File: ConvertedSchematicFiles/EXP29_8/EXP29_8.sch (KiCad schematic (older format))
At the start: 25 parts, among them U1 uA741, U2 uA741

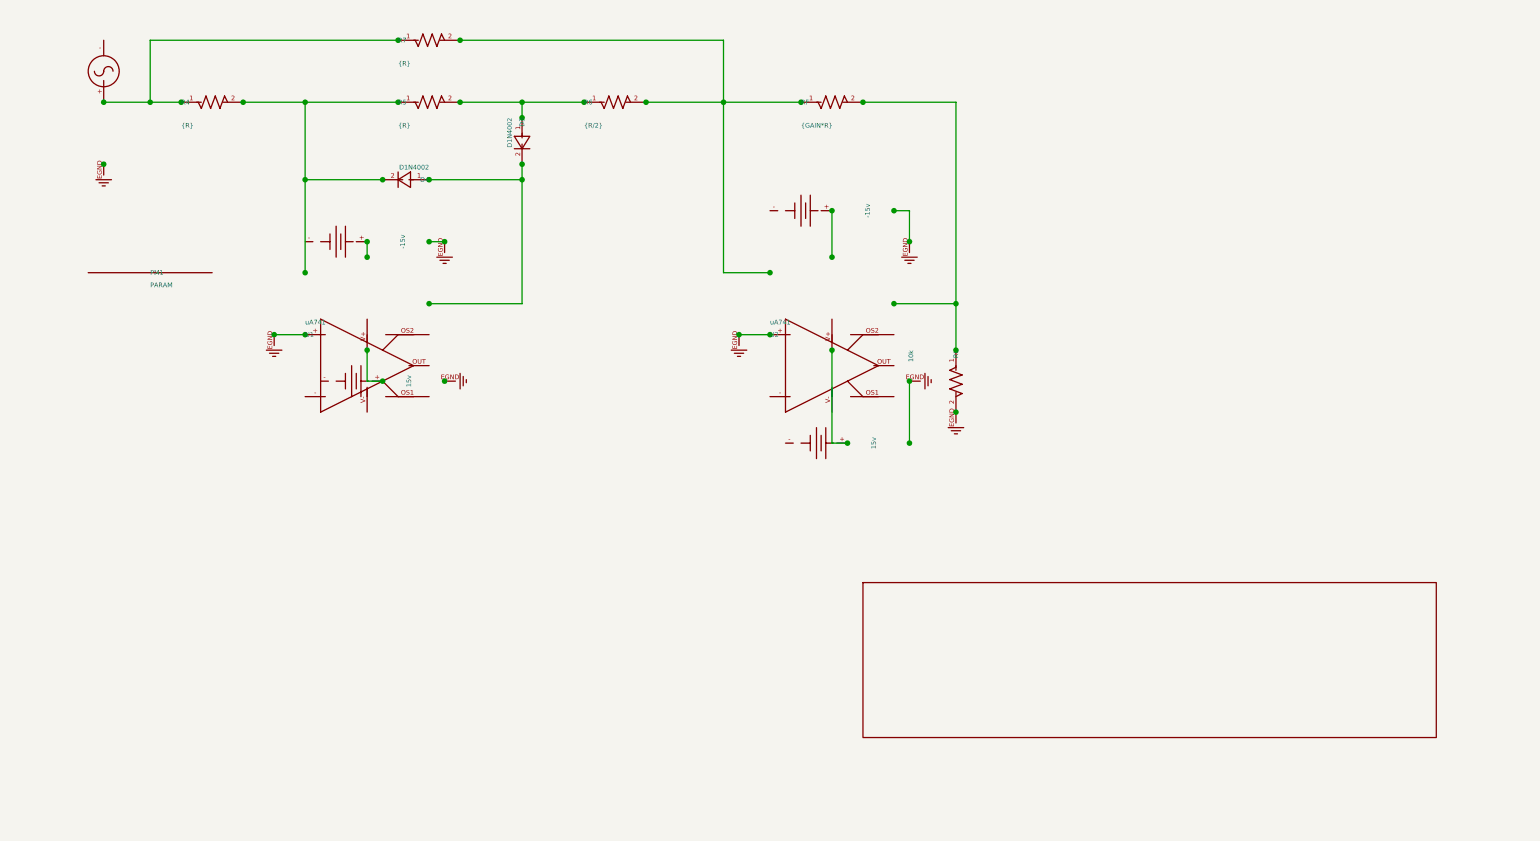
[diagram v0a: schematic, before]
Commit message: Excluded some components. These no longer appear after conversion. When calling shell commands, filenames are in "quotes"
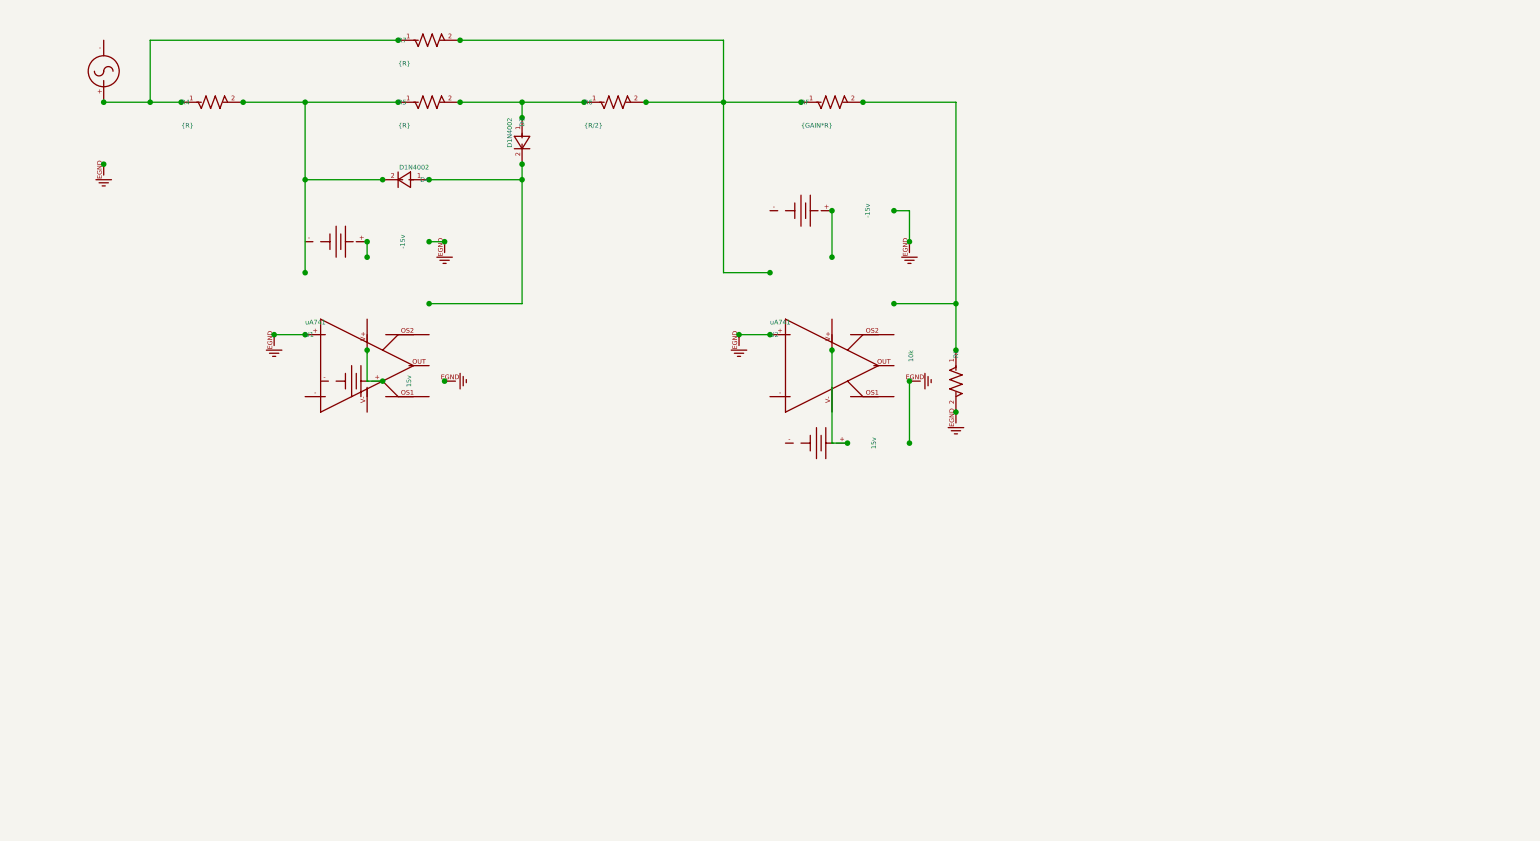
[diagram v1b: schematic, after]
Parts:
- removed PM1: PARAM, symbol PARAM_PSPICE
- removed titleblk: titleblk, symbol TITLEBLK_PSPICE
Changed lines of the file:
@@
 	-1    0    0    -1
-$EndComp
-$Comp
-L PARAM_PSPICE PM1
-U 1 1 26956429
-P 1400 4200
-F 0 "PM1" H 1400 4200 30  0000 L CNN
-F 1 "PARAM" H 1400 4280 30  0000 L CNN
-	1    1400 4200
-	1    0    0    1
-$EndComp
-$Comp
-L TITLEBLK_PSPICE titleblk
-U 1 1 76465782
-P 9700 7200
-F 0 "titleblk" H 19400 14400 30  0001 L CNN
-F 1 "titleblk" H 19400 14480 30  0001 L CNN
-	1    9700 7200
-	1    0    0    1
 $EndComp
 Wire Wire Line

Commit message: Ports issue fixed. Now annotation for ports is #PWR? function added "itos"
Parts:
- removed EGND (x3): EGND, symbol EGND_PSPICE
- removed GND_EARTH (x5): GND_EARTH, symbol GND_EARTH_PSPICE
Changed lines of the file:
@@
 $EndDescr
 $Comp
-L GND_EARTH_PSPICE GND_EARTH
+L GND_EARTH_PSPICE #PWR1
 U 1 1 14289383
 P 3300 4900
-F 0 "GND_EARTH" H 6600 9800 30  0001 L CNN
+F 0 "#PWR1" H 6600 9800 30  0001 L CNN
 F 1 "GND_EARTH" H 6600 9880 30  0001 L CNN
 	1    3300 4900
@@
 $EndComp
 $Comp
-L GND_EARTH_PSPICE GND_EARTH
+L GND_EARTH_PSPICE #PWR2
 U 1 1 46930886
 P 3300 4000
-F 0 "GND_EARTH" H 6600 8000 30  0001 L CNN
+F 0 "#PWR2" H 6600 8000 30  0001 L CNN
 F 1 "GND_EARTH" H 6600 8080 30  0001 L CNN
 	1    3300 4000
@@
 $EndComp
 $Comp
-L GND_EARTH_PSPICE GND_EARTH
+L GND_EARTH_PSPICE #PWR3
 U 1 1 71692777
 P 1100 3500
-F 0 "GND_EARTH" H 2200 7000 30  0001 L CNN
+F 0 "#PWR3" H 2200 7000 30  0001 L CNN
 F 1 "GND_EARTH" H 2200 7080 30  0001 L CNN
 	1    1100 3500
@@
 $EndComp
 $Comp
-L EGND_PSPICE EGND
+L EGND_PSPICE #PWR4
 U 1 1 14636915
 P 6600 5100
-F 0 "EGND" H 13200 10200 30  0001 L CNN
+F 0 "#PWR4" H 13200 10200 30  0001 L CNN
 F 1 "EGND" H 13200 10280 30  0001 L CNN
 	1    6600 5100
@@
 $EndComp
 $Comp
-L EGND_PSPICE EGND
+L EGND_PSPICE #PWR5
 U 1 1 77747793
 P 2200 4600
-F 0 "EGND" H 4400 9200 30  0001 L CNN
+F 0 "#PWR5" H 4400 9200 30  0001 L CNN
 F 1 "EGND" H 4400 9280 30  0001 L CNN
 	1    2200 4600
@@
 $EndComp
 $Comp
-L EGND_PSPICE EGND
+L EGND_PSPICE #PWR6
 U 1 1 74238335
 P 5200 4600
-F 0 "EGND" H 10400 9200 30  0001 L CNN
+F 0 "#PWR6" H 10400 9200 30  0001 L CNN
 F 1 "EGND" H 10400 9280 30  0001 L CNN
 	1    5200 4600
@@
 $EndComp
 $Comp
-L GND_EARTH_PSPICE GND_EARTH
+L GND_EARTH_PSPICE #PWR7
 U 1 1 99885386
 P 6300 4000
-F 0 "GND_EARTH" H 12600 8000 30  0001 L CNN
+F 0 "#PWR7" H 12600 8000 30  0001 L CNN
 F 1 "GND_EARTH" H 12600 8080 30  0001 L CNN
 	1    6300 4000
@@
 $EndComp
 $Comp
-L GND_EARTH_PSPICE GND_EARTH
+L GND_EARTH_PSPICE #PWR8
 U 1 1 39760492
 P 6300 4900
-F 0 "GND_EARTH" H 12600 9800 30  0001 L CNN
+F 0 "#PWR8" H 12600 9800 30  0001 L CNN
 F 1 "GND_EARTH" H 12600 9880 30  0001 L CNN
 	1    6300 4900

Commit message: Added LICENSE.txt
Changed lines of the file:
@@
 $EndDescr
 $Comp
-L GND_EARTH_PSPICE #PWR1
+L GND #PWR1
 U 1 1 14289383
 P 3300 4900
@@
 $EndComp
 $Comp
-L GND_EARTH_PSPICE #PWR2
+L GND #PWR2
 U 1 1 46930886
 P 3300 4000
@@
 $EndComp
 $Comp
-L GND_EARTH_PSPICE #PWR3
+L GND #PWR3
 U 1 1 71692777
 P 1100 3500
@@
 $EndComp
 $Comp
-L EGND_PSPICE #PWR4
+L GND #PWR4
 U 1 1 14636915
 P 6600 5100
@@
 $EndComp
 $Comp
-L EGND_PSPICE #PWR5
+L GND #PWR5
 U 1 1 77747793
 P 2200 4600
@@
 $EndComp
 $Comp
-L EGND_PSPICE #PWR6
+L GND #PWR6
 U 1 1 74238335
 P 5200 4600
@@
 $EndComp
 $Comp
-L GND_EARTH_PSPICE #PWR7
+L GND #PWR7
 U 1 1 99885386
 P 6300 4000
@@
 $EndComp
 $Comp
-L GND_EARTH_PSPICE #PWR8
+L GND #PWR8
 U 1 1 39760492
 P 6300 4900

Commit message: Orientation fix. Library components are now inverted, with +ve y axis going up. In Schematic files, +ve y axis is downwards. This is how the KiCad libraries are. As a result of the above fixed, the converted GND is now oriented correctly.
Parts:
- VIN: value VSIN -> SINE
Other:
- moved on the sheet: U1, U2
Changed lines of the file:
@@
 F 1 "GND_EARTH" H 6600 9880 30  0001 L CNN
 	1    3300 4900
-	0    1    -1    0
+	0    -1    -1    0
 $EndComp
 $Comp
@@
 F 1 "GND_EARTH" H 6600 8080 30  0001 L CNN
 	1    3300 4000
-	1    0    0    1
+	1    0    0    -1
 $EndComp
 $Comp
@@
 F 1 "GND_EARTH" H 2200 7080 30  0001 L CNN
 	1    1100 3500
-	1    0    0    1
+	1    0    0    -1
 $EndComp
 $Comp
@@
 F 1 "EGND" H 13200 10280 30  0001 L CNN
 	1    6600 5100
-	1    0    0    1
+	1    0    0    -1
 $EndComp
 $Comp
@@
 F 1 "EGND" H 4400 9280 30  0001 L CNN
 	1    2200 4600
-	1    0    0    1
+	1    0    0    -1
 $EndComp
 $Comp
@@
 F 1 "EGND" H 10400 9280 30  0001 L CNN
 	1    5200 4600
-	1    0    0    1
+	1    0    0    -1
 $EndComp
 $Comp
@@
 F 1 "GND_EARTH" H 12600 8080 30  0001 L CNN
 	1    6300 4000
-	1    0    0    1
+	1    0    0    -1
 $EndComp
 $Comp
@@
 F 1 "GND_EARTH" H 12600 9880 30  0001 L CNN
 	1    6300 4900
-	0    1    -1    0
+	0    -1    -1    0
 $EndComp
 $Comp
@@
 F 1 "15v" H 2900 5070 30  0000 C CNN
 	1    2900 4900
-	0    1    -1    0
+	0    -1    -1    0
 $EndComp
 $Comp
@@
 F 1 "-15v" H 2800 4230 30  0000 C CNN
 	1    2800 4000
-	0    1    -1    0
+	0    -1    -1    0
 $EndComp
 $Comp
@@
 F 1 "D1N4002" H 3800 3280 30  0000 L CNN
 	1    3800 3200
-	0    -1    1    0
+	0    1    1    0
 $EndComp
 $Comp
@@
 F 1 "10k" H 6600 4990 30  0000 L CNN
 	1    6600 4700
-	0    -1    1    0
+	0    1    1    0
 $EndComp
 $Comp
@@
 F 1 "{R}" H 1600 3250 30  0000 L CNN
 	1    1600 3100
-	1    0    0    1
+	1    0    0    -1
 $EndComp
 $Comp
@@
 F 1 "{R}" H 3000 3250 30  0000 L CNN
 	1    3000 3100
-	1    0    0    1
+	1    0    0    -1
 $EndComp
 $Comp
@@
 P 1100 3100
 F 0 "VIN" H 1100 3100 30  0001 L CNN
-F 1 "VSIN" H 1100 3180 30  0001 L CNN
+F 1 "SINE" H 1100 3180 30  0001 L CNN
 	1    1100 3100
-	1    0    0    1
+	1    0    0    -1
 $EndComp
 $Comp
@@
 F 1 "{GAIN*R}" H 5600 3250 30  0000 L CNN
 	1    5600 3100
-	1    0    0    1
+	1    0    0    -1
 $EndComp
 $Comp
@@
 F 1 "-15v" H 5800 4030 30  0000 C CNN
 	1    5800 3800
-	0    1    -1    0
+	0    -1    -1    0
 $EndComp
 $Comp
@@
 F 1 "15v" H 5900 5470 30  0000 C CNN
 	1    5900 5300
-	0    1    -1    0
+	0    -1    -1    0
 $EndComp
 $Comp
@@
 F 1 "uA741" H 5400 4680 30  0000 L CNN
 	1    5400 4600
-	1    0    0    -1
+	1    0    0    1
 $EndComp
 $Comp
@@
 F 1 "{R/2}" H 4200 3250 30  0000 L CNN
 	1    4200 3100
-	1    0    0    1
+	1    0    0    -1
 $EndComp
 $Comp
@@
 F 1 "{R}" H 3000 2850 30  0000 L CNN
 	1    3000 2700
-	1    0    0    1
+	1    0    0    -1
 $EndComp
 $Comp
@@
 F 1 "uA741" H 2400 4680 30  0000 L CNN
 	1    2400 4600
-	1    0    0    -1
+	1    0    0    1
 $EndComp
 $Comp
@@
 F 1 "D1N4002" H 3200 3680 30  0000 L CNN
 	1    3200 3600
-	-1    0    0    -1
+	-1    0    0    1
 $EndComp
 Wire Wire Line

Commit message: Removed the use of exec, wrote basename function, made integration with eSim easier.
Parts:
- added PM1: PARAM, symbol PARAM_PSPICE
- added titleblk: titleblk, symbol titleblk_PSPICE
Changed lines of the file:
@@
-EESchema Schematic File Version 2  date Friday 18 February 2000 11:41:50 PM IST
+EESchema Schematic File Version 2  date
 LIBS:power
 LIBS:device
@@
 LIBS:contrib
 LIBS:valves
-LIBS:ConvertedSchematicFiles/EXP29_8-cache
 EELAYER 25  0
 EELAYER END
@@
 Sheet 1 1
 Title ""
-Date "18 Feb 2000"
+Date ""
 Rev ""
 Comp ""
@@
 	-1    0    0    1
 $EndComp
+$Comp
+L PARAM_PSPICE PM1
+U 1 1 26956429
+P 1400 4200
+F 0 "PM1" H 1400 4200 30  0000 L CNN
+F 1 "PARAM" H 1400 4280 30  0000 L CNN
+	1    1400 4200
+	1    0    0    -1
+$EndComp
+$Comp
+L titleblk_PSPICE titleblk
+U 1 1 76465782
+P 9700 7200
+F 0 "titleblk" H 19400 14400 30  0001 L CNN
+F 1 "titleblk" H 19400 14480 30  0001 L CNN
+	1    9700 7200
+	1    0    0    -1
+$EndComp
 Wire Wire Line
